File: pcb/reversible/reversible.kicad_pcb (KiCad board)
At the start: 2 copper layers, 29 parts

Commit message: started reversible pcb project
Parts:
- removed the REF** at (145.5, 133.5)
- removed the REF** at (145.5, 57.5)
- removed the REF** at (202.5, 95.5)
- removed the REF** at (164.5, 114.5)
- removed the REF** at (126.5, 57.5)
- removed the REF** at (126.5, 95.5)
- removed the REF** at (183.5, 76.5)
- removed the REF** at (126.5, 76.5)
- removed the REF** at (164.5, 76.5)
- removed the REF** at (164.5, 95.5)
- removed the REF** at (164.5, 57.5)
- removed the REF** at (183.5, 114.5)
- removed the REF** at (202.5, 76.5)
- removed the REF** at (107.5, 133.5)
- removed the REF** at (86.4, 127.8)
- removed the REF** at (145.5, 114.5)
- removed the REF** at (145.5, 76.5)
- removed the REF** at (183.5, 95.5)
- removed the REF** at (86.4, 108.8)
- removed the REF** at (183.5, 57.5)
- removed the REF** at (202.5, 57.5)
- removed the REF** at (145.5, 95.5)
- removed the REF** at (126.5, 114.5)
- removed the REF** at (107.5, 95.5)
- removed the REF** at (126.5, 133.5)
- removed the REF** at (107.5, 76.5)
- removed the REF** at (107.5, 114.5)
- removed the REF** at (202.5, 114.5)
- removed the REF** at (107.5, 57.5)
- added J2: 5PIN, lowProfile:TRRS_JACK_MJ4PP9, F.Cu at (188.5, 85.4)
- added REF**: Gateron_Low_Profile_Socket, lowProfileSplit:Gateron_Low_Profile_Socket, F.Cu at (104.0, 68.0)
- added REF**: Gateron_Low_Profile_Socket, lowProfileSplit:Gateron_Low_Profile_Socket, F.Cu at (123.0, 85.5)
- added REF**: Gateron_Low_Profile_Socket, lowProfileSplit:Gateron_Low_Profile_Socket, F.Cu at (142.0, 106.0)
- added REF**: Gateron_Low_Profile_Socket, lowProfileSplit:Gateron_Low_Profile_Socket, F.Cu at (66.0, 109.0)
- added REF**: Gateron_Low_Profile_Socket, lowProfileSplit:Gateron_Low_Profile_Socket, F.Cu at (104.0, 87.0)
- added REF**: Gateron_Low_Profile_Socket, lowProfileSplit:Gateron_Low_Profile_Socket, F.Cu at (161.0, 88.5)
- added REF**: Gateron_Low_Profile_Socket, lowProfileSplit:Gateron_Low_Profile_Socket, F.Cu at (104.0, 49.0)
- added REF**: Gateron_Low_Profile_Socket, lowProfileSplit:Gateron_Low_Profile_Socket, F.Cu at (161.0, 69.5)
- added REF**: Gateron_Low_Profile_Socket, lowProfileSplit:Gateron_Low_Profile_Socket, F.Cu at (180.0, 100.0)
- added REF**: Gateron_Low_Profile_Socket, lowProfileSplit:Gateron_Low_Profile_Socket, F.Cu at (66.0, 90.0)
- added REF**: Gateron_Low_Profile_Socket, lowProfileSplit:Gateron_Low_Profile_Socket, F.Cu at (161.0, 107.5)
- added REF**: Gateron_Low_Profile_Socket, lowProfileSplit:Gateron_Low_Profile_Socket, F.Cu at (142.0, 126.5)
- added REF**: Gateron_Low_Profile_Socket, lowProfileSplit:Gateron_Low_Profile_Socket, F.Cu at (123.0, 66.5)
- added REF**: Gateron_Low_Profile_Socket, lowProfileSplit:Gateron_Low_Profile_Socket, F.Cu at (66.0, 71.0)
- added REF**: Gateron_Low_Profile_Socket, lowProfileSplit:Gateron_Low_Profile_Socket, F.Cu at (85.0, 50.5)
- added REF**: Gateron_Low_Profile_Socket, lowProfileSplit:Gateron_Low_Profile_Socket, F.Cu at (142.0, 68.0)
- added REF**: Gateron_Low_Profile_Socket, lowProfileSplit:Gateron_Low_Profile_Socket, F.Cu at (142.0, 87.0)
- added REF**: Gateron_Low_Profile_Socket, lowProfileSplit:Gateron_Low_Profile_Socket, F.Cu at (85.0, 107.5)
- added REF**: Gateron_Low_Profile_Socket, lowProfileSplit:Gateron_Low_Profile_Socket, F.Cu at (85.0, 88.5)
- added REF**: Gateron_Low_Profile_Socket, lowProfileSplit:Gateron_Low_Profile_Socket, F.Cu at (123.0, 104.5)
- added REF**: Gateron_Low_Profile_Socket, lowProfileSplit:Gateron_Low_Profile_Socket, F.Cu at (104.0, 106.0)
- added REF**: Gateron_Low_Profile_Socket, lowProfileSplit:Gateron_Low_Profile_Socket, F.Cu at (142.0, 49.0)
- added REF**: Gateron_Low_Profile_Socket, lowProfileSplit:Gateron_Low_Profile_Socket, F.Cu at (123.0, 47.5)
- added REF**: Gateron_Low_Profile_Socket, lowProfileSplit:Gateron_Low_Profile_Socket, F.Cu at (85.0, 69.5)
- added REF**: Gateron_Low_Profile_Socket, lowProfileSplit:Gateron_Low_Profile_Socket, F.Cu at (180.0, 119.0)
- added REF**: Gateron_Low_Profile_Socket, lowProfileSplit:Gateron_Low_Profile_Socket, F.Cu at (66.0, 52.0)
- added REF**: Gateron_Low_Profile_Socket, lowProfileSplit:Gateron_Low_Profile_Socket, F.Cu at (161.4, 126.5)
- added REF**: Gateron_Low_Profile_Socket, lowProfileSplit:Gateron_Low_Profile_Socket, F.Cu at (123.0, 126.5)
- added REF**: Gateron_Low_Profile_Socket, lowProfileSplit:Gateron_Low_Profile_Socket, F.Cu at (161.0, 50.5)
- added U1: ProMicro, lowProfile:ProMicro_rev, F.Cu at (181.6, 59.5)

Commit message: layout designed
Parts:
- removed J2: 5PIN, lowProfile:TRRS_JACK_MJ4PP9
- removed REF** (x29): Gateron_Low_Profile_Socket, lowProfileSplit:Gateron_Low_Profile_Socket
- added C1: 100nF, lowProfile:RESISTOR, F.Cu at (79.5, 60.6)
- added C2: 100nF, lowProfile:RESISTOR, F.Cu at (79.5, 74.1)
- added D1: 1N4148/1N4148W, lowProfile:Diode_TH_SOD123, F.Cu at (91.5, 50.0)
- added D10: 1N4148/1N4148W, lowProfile:Diode_TH_SOD123, F.Cu at (72.5, 126.0)
- added D11: 1N4148/1N4148W, lowProfile:Diode_TH_SOD123, F.Cu at (129.5, 47.0)
- added D12: 1N4148/1N4148W, lowProfile:Diode_TH_SOD123, F.Cu at (129.5, 66.0)
- added D13: 1N4148/1N4148W, lowProfile:Diode_TH_SOD123, F.Cu at (129.5, 85.0)
- added D14: 1N4148/1N4148W, lowProfile:Diode_TH_SOD123, F.Cu at (129.5, 104.0)
- added D15: 1N4148/1N4148W, lowProfile:Diode_TH_SOD123, F.Cu at (91.5, 126.0)
- added D16: 1N4148/1N4148W, lowProfile:Diode_TH_SOD123, F.Cu at (148.5, 48.5)
- added D17: 1N4148/1N4148W, lowProfile:Diode_TH_SOD123, F.Cu at (148.5, 67.5)
- added D18: 1N4148/1N4148W, lowProfile:Diode_TH_SOD123, F.Cu at (148.5, 86.5)
- added D19: 1N4148/1N4148W, lowProfile:Diode_TH_SOD123, F.Cu at (148.5, 105.5)
- added D2: 1N4148/1N4148W, lowProfile:Diode_TH_SOD123, F.Cu at (91.7, 69.0)
- added D20: 1N4148/1N4148W, lowProfile:Diode_TH_SOD123, F.Cu at (110.5, 126.0)
- added D21: 1N4148/1N4148W, lowProfile:Diode_TH_SOD123, F.Cu at (167.5, 50.0)
- added D22: 1N4148/1N4148W, lowProfile:Diode_TH_SOD123, F.Cu at (167.5, 69.0)
- added D23: 1N4148/1N4148W, lowProfile:Diode_TH_SOD123, F.Cu at (167.5, 88.0)
- added D24: 1N4148/1N4148W, lowProfile:Diode_TH_SOD123, F.Cu at (167.5, 107.0)
- added D25: 1N4148/1N4148W, lowProfile:Diode_TH_SOD123, F.Cu at (129.5, 126.0)
- added D26: 1N4148/1N4148W, lowProfile:Diode_TH_SOD123, F.Cu at (186.5, 51.5)
- added D27: 1N4148/1N4148W, lowProfile:Diode_TH_SOD123, F.Cu at (186.5, 70.5)
- added D28: 1N4148/1N4148W, lowProfile:Diode_TH_SOD123, F.Cu at (186.5, 89.5)
- added D29: 1N4148/1N4148W, lowProfile:Diode_TH_SOD123, F.Cu at (186.5, 108.5)
- added D3: 1N4148/1N4148W, lowProfile:Diode_TH_SOD123, F.Cu at (91.5, 88.0)
- added D30: 1N4148/1N4148W, lowProfile:Diode_TH_SOD123, F.Cu at (66.3, 91.5)
- added D4: 1N4148/1N4148W, lowProfile:Diode_TH_SOD123, F.Cu at (91.5, 107.0)
- added D5: 1N4148/1N4148W, lowProfile:Diode_TH_SOD123, F.Cu at (66.5, 107.0)
- added D6: 1N4148/1N4148W, lowProfile:Diode_TH_SOD123, F.Cu at (110.5, 48.5)
- added D7: 1N4148/1N4148W, lowProfile:Diode_TH_SOD123, F.Cu at (110.5, 67.5)
- added D8: 1N4148/1N4148W, lowProfile:Diode_TH_SOD123, F.Cu at (110.5, 86.5)
- added D9: 1N4148/1N4148W, lowProfile:Diode_TH_SOD123, F.Cu at (110.5, 105.5)
- added J1: PJ-320A, lowProfile:TRRS_JACK_MJ4PP9, F.Cu at (57.2, 98.1)
- added JP1: RESET, lowProfile:Jumper, B.Cu at (60.5, 46.5)
- added JP10: Jumper_NO_Small, lowProfile:Jumper, B.Cu at (70.0, 84.5)
- added JP11: LEFT, lowProfile:Jumper, F.Cu at (58.0, 84.5)
- added JP12: RIGHT, lowProfile:Jumper, B.Cu at (58.0, 84.5)
- added JP2: RESET, lowProfile:Jumper, F.Cu at (60.5, 46.5)
- added JP3: Jumper_NO_Small, lowProfile:Jumper, F.Cu at (62.5, 84.5)
- added JP4: Jumper_NO_Small, lowProfile:Jumper, F.Cu at (65.0, 84.5)
- added JP5: Jumper_NO_Small, lowProfile:Jumper, F.Cu at (67.5, 84.5)
- added JP6: Jumper_NO_Small, lowProfile:Jumper, F.Cu at (70.0, 84.5)
- added JP7: Jumper_NO_Small, lowProfile:Jumper, B.Cu at (62.5, 84.5)
- added JP8: Jumper_NO_Small, lowProfile:Jumper, B.Cu at (65.0, 84.5)
- added JP9: Jumper_NO_Small, lowProfile:Jumper, B.Cu at (67.5, 84.5)
- added P1: OLED, lowProfile:OLED_4Pin, F.Cu at (62.5, 87.5)
- added R1: 4k7, Resistor_THT:R_Axial_DIN0207_L6.3mm_D2.5mm_P7.62mm_Horizontal, F.Cu at (78.5, 91.6)
- added R2: 4k7, Resistor_THT:R_Axial_DIN0207_L6.3mm_D2.5mm_P7.62mm_Horizontal, F.Cu at (78.5, 102.3)
- added SW1: Kailh hotswap MX socket, lowProfile:Gateron_Low_Profile_Socket, F.Cu at (91.5, 59.5)
- added SW10: Kailh hotswap MX socket, lowProfile:Gateron_Low_Profile_Socket, F.Cu at (72.6, 135.5)
- added SW11: Kailh hotswap MX socket, lowProfile:Gateron_Low_Profile_Socket, F.Cu at (129.5, 56.5)
- added SW12: Kailh hotswap MX socket, lowProfile:Gateron_Low_Profile_Socket, F.Cu at (129.5, 75.5)
- added SW13: Kailh hotswap MX socket, lowProfile:Gateron_Low_Profile_Socket, F.Cu at (129.5, 94.5)
- added SW14: Kailh hotswap MX socket, lowProfile:Gateron_Low_Profile_Socket, F.Cu at (129.5, 113.5)
- added SW15: Kailh hotswap MX socket, lowProfile:Gateron_Low_Profile_Socket, F.Cu at (91.5, 135.5)
- added SW16: Kailh hotswap MX socket, lowProfile:Gateron_Low_Profile_Socket, F.Cu at (148.5, 58.0)
- added SW17: Kailh hotswap MX socket, lowProfile:Gateron_Low_Profile_Socket, F.Cu at (148.5, 77.0)
- added SW18: Kailh hotswap MX socket, lowProfile:Gateron_Low_Profile_Socket, F.Cu at (148.5, 96.1)
- added SW19: Kailh hotswap MX socket, lowProfile:Gateron_Low_Profile_Socket, F.Cu at (148.5, 115.0)
- added SW2: Kailh hotswap MX socket, lowProfile:Gateron_Low_Profile_Socket, F.Cu at (91.5, 78.5)
- added SW20: Kailh hotswap MX socket, lowProfile:Gateron_Low_Profile_Socket, F.Cu at (110.5, 135.5)
- added SW21: Kailh hotswap MX socket, lowProfile:Gateron_Low_Profile_Socket, F.Cu at (167.5, 59.5)
- added SW22: Kailh hotswap MX socket, lowProfile:Gateron_Low_Profile_Socket, F.Cu at (167.5, 78.5)
- added SW23: Kailh hotswap MX socket, lowProfile:Gateron_Low_Profile_Socket, F.Cu at (167.5, 97.5)
- added SW24: Kailh hotswap MX socket, lowProfile:Gateron_Low_Profile_Socket, F.Cu at (167.5, 116.5)
- added SW25: Kailh hotswap MX socket, lowProfile:Gateron_Low_Profile_Socket, F.Cu at (129.5, 135.5)
- added SW26: Kailh hotswap MX socket, lowProfile:Gateron_Low_Profile_Socket, F.Cu at (186.6, 61.0)
- added SW27: Kailh hotswap MX socket, lowProfile:Gateron_Low_Profile_Socket, F.Cu at (186.5, 80.0)
- added SW28: Kailh hotswap MX socket, lowProfile:Gateron_Low_Profile_Socket, F.Cu at (186.5, 99.0)
- added SW29: Kailh hotswap MX socket, lowProfile:Gateron_Low_Profile_Socket, F.Cu at (186.5, 118.0)
- added SW3: Kailh hotswap MX socket, lowProfile:Gateron_Low_Profile_Socket, F.Cu at (91.5, 97.5)
- added SW30: Rotary_Encoder_Switch, lowProfile:RotaryEncoder_Alps_EC12E-Switch_Vertical_H20mm, F.Cu at (66.1, 66.2)
- added SW4: Kailh hotswap MX socket, lowProfile:Gateron_Low_Profile_Socket, F.Cu at (91.5, 116.5)
- added SW5: Kailh hotswap MX socket, lowProfile:Gateron_Low_Profile_Socket, F.Cu at (66.5, 116.5)
- added SW6: Kailh hotswap MX socket, lowProfile:Gateron_Low_Profile_Socket, F.Cu at (110.5, 58.0)
- added SW7: Kailh hotswap MX socket, lowProfile:Gateron_Low_Profile_Socket, F.Cu at (110.5, 77.0)
- added SW8: Kailh hotswap MX socket, lowProfile:Gateron_Low_Profile_Socket, F.Cu at (110.5, 96.0)
- added SW9: Kailh hotswap MX socket, lowProfile:Gateron_Low_Profile_Socket, F.Cu at (110.5, 115.0)
- added TH1: HOLE, MountingHole:MountingHole_3.7mm, F.Cu at (79.5, 49.0)
- added TH2: HOLE, MountingHole:MountingHole_3.7mm, F.Cu at (178.0, 48.5)
- added TH3: HOLE, MountingHole:MountingHole_3.7mm, F.Cu at (59.0, 139.0)
- added TH4: HOLE, MountingHole:MountingHole_3.7mm, F.Cu at (177.0, 122.5)
- added TH5: HOLE, MountingHole:MountingHole_3.7mm, F.Cu at (120.0, 84.0)
- U1: footprint lowProfile:ProMicro_rev -> lowProfile:ProMicro_rev2
- moved U1 115.3 mm to (66.5, 66.6)
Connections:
- U1 pad 1: (no net) -> unconnected-(U1-TX0/PD3-Pad1)
- U1 pad 10: (no net) -> row3
- U1 pad 11: (no net) -> row4
- U1 pad 12: (no net) -> Hand
- U1 pad 13: (no net) -> col3
- U1 pad 14: (no net) -> col1
- U1 pad 15: (no net) -> col2
- U1 pad 16: (no net) -> col0
- U1 pad 17: (no net) -> col4
- U1 pad 18: (no net) -> col5
- U1 pad 19: (no net) -> A
- U1 pad 2: (no net) -> DATA
- U1 pad 20: (no net) -> B
- U1 pad 21: (no net) -> VCC
- U1 pad 22: (no net) -> RESET
- U1 pad 23: (no net) -> GND
- U1 pad 24: (no net) -> unconnected-(U1-RAW-Pad24)
- U1 pad 3: (no net) -> GND
- U1 pad 4: (no net) -> GND
- U1 pad 5: (no net) -> SDA
- U1 pad 6: (no net) -> SCL
- U1 pad 7: (no net) -> row0
- U1 pad 8: (no net) -> row1
- U1 pad 9: (no net) -> row2
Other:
- board outline added: 139.5 x 98.5 mm

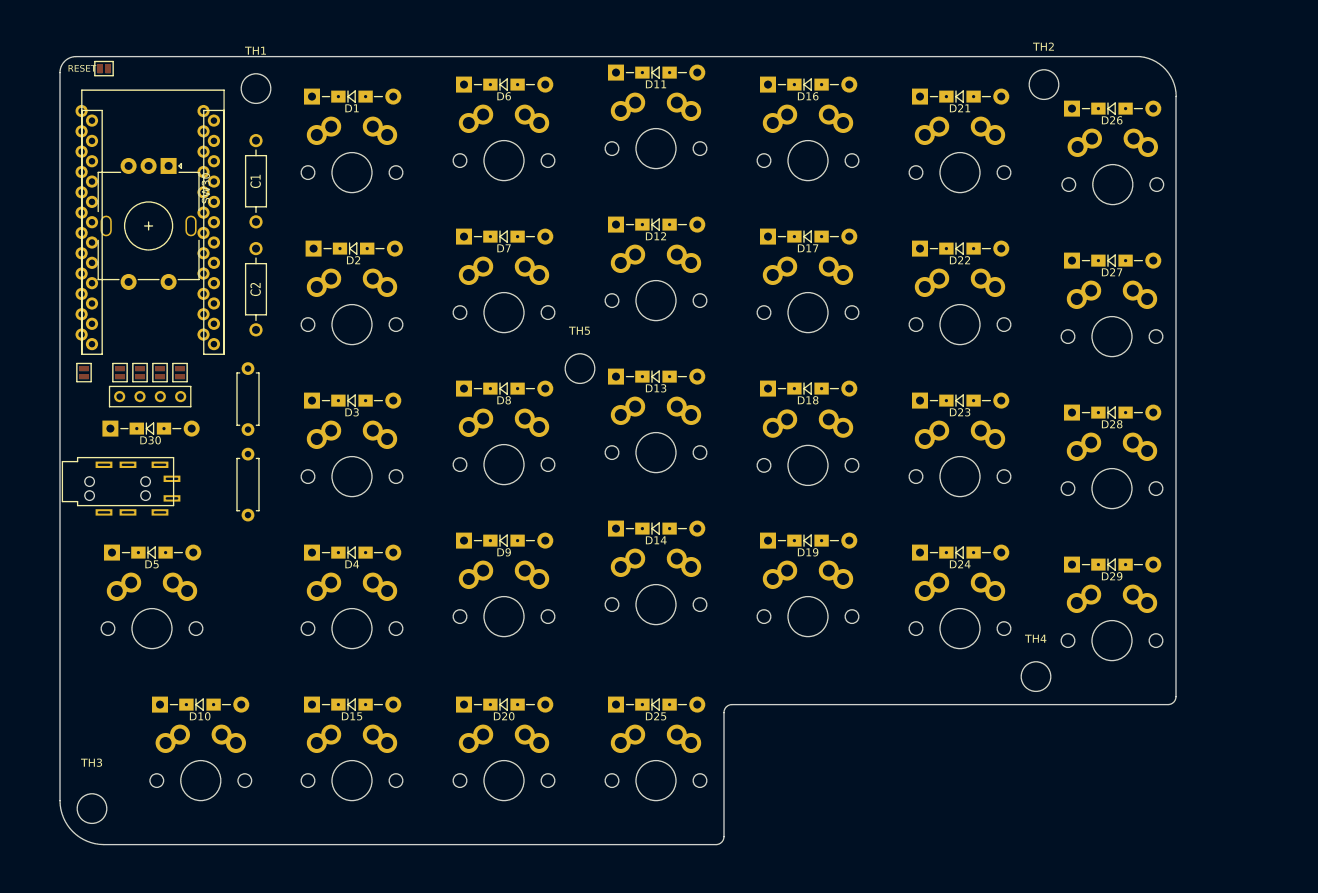
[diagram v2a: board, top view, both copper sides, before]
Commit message: matrix routed
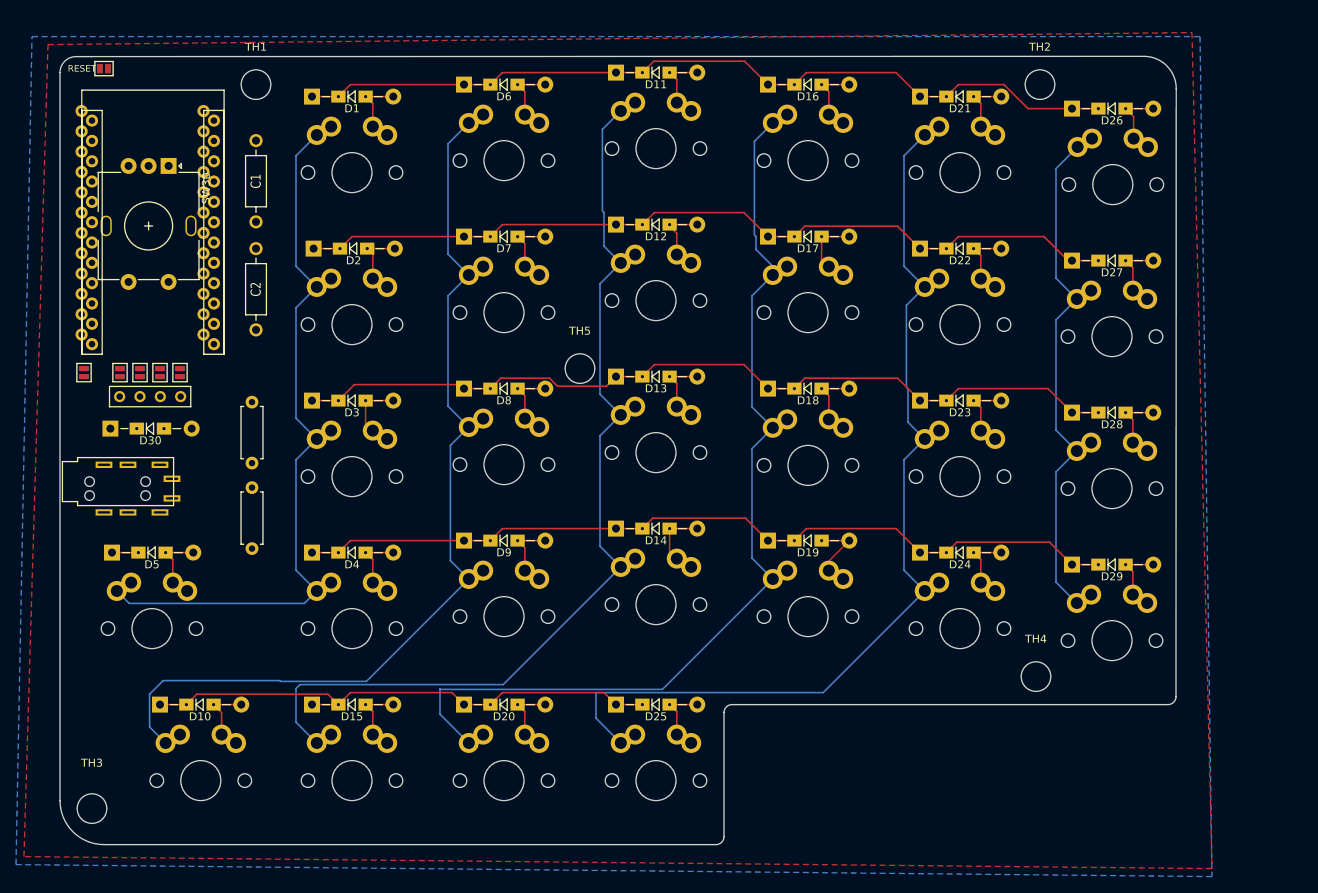
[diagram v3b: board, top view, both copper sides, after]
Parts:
- moved R1 4.22 mm to (79.0, 95.8)
- moved R2 3.47 mm to (79.0, 98.9), turned to -90 degrees
- moved TH1 0.50 mm to (79.5, 48.5)
- moved TH2 0.50 mm to (177.5, 48.5)
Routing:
- net col2: track 0.00 -> 130.8 mm
- net col3: track 0.00 -> 129.2 mm
- net col1: track 0.00 -> 128.3 mm
- net col4: track 0.00 -> 127.3 mm
- net row2: track 0.00 -> 106.2 mm
- net row0: track 0.00 -> 105.1 mm
- net row3: track 0.00 -> 104.8 mm
- net row1: track 0.00 -> 104.8 mm
- net col5: track 0.00 -> 100.9 mm
- net col0: track 0.00 -> 72.4 mm
- net row4: track 0.00 -> 70.5 mm
- net Net-(D19-A): track 0.00 -> 10.5 mm
- net Net-(D18-A): track 0.00 -> 9.92 mm
- net Net-(D26-A): track 0.00 -> 9.86 mm
- net Net-(D10-A): track 0.00 -> 9.86 mm
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- added copper zone on B.Cu, net GND
- added copper zone on F.Cu, net GND
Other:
- outline, holes or cut-outs redrawn

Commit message: fixed missing GND connections
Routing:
- net col0: track 72.4 -> 202.0 mm, vias 0 -> 1
- net col1: track 128.3 -> 234.9 mm, vias 0 -> 2
- net SDA: track 0.00 -> 95.0 mm, vias 0 -> 3
- net col2: track 130.8 -> 221.5 mm, vias 0 -> 2
- net VCC: track 0.00 -> 85.1 mm, vias 0 -> 3
- net row4: track 70.5 -> 144.9 mm, vias 0 -> 2
- net SCL: track 0.00 -> 67.7 mm, vias 0 -> 3
- net DATA: track 0.00 -> 67.6 mm
- net col3: track 129.2 -> 194.1 mm, vias 0 -> 3
- net row3: track 104.8 -> 164.6 mm, vias 0 -> 1
- net col4: track 127.3 -> 174.0 mm, vias 0 -> 1
- net row2: track 106.2 -> 149.8 mm, vias 0 -> 1
- net row0: track 105.1 -> 148.6 mm, vias 0 -> 1
- net row1: track 104.8 -> 137.0 mm, vias 0 -> 1
- net col5: track 100.9 -> 131.1 mm, vias 0 -> 2
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
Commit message: gerber files
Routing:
- net DATA: track 67.6 -> 77.4 mm
- net col4: track 174.0 -> 166.6 mm
- net SDA: track 95.0 -> 89.3 mm, vias 3 -> 4
- net col2: track 221.5 -> 216.1 mm, vias 2 -> 3
- net col1: track 234.9 -> 229.7 mm, vias 2 -> 3
- net row2: track 149.8 -> 145.6 mm
- net VCC: track 85.1 -> 82.1 mm
- net row3: track 164.6 -> 161.8 mm
- net col0: track 202.0 -> 199.9 mm
- net row0: track 148.6 -> 146.5 mm
- net col5: track 131.1 -> 129.2 mm
- net row1: track 137.0 -> 135.3 mm
- net Hand: track 23.6 -> 22.4 mm
- net A: track 28.6 -> 29.3 mm
- net GND: vias 0 -> 13
